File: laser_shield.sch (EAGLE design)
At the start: 18 parts, among them IC1 74AC08N, U1 ARDUINO_SHIELDLONGPADS

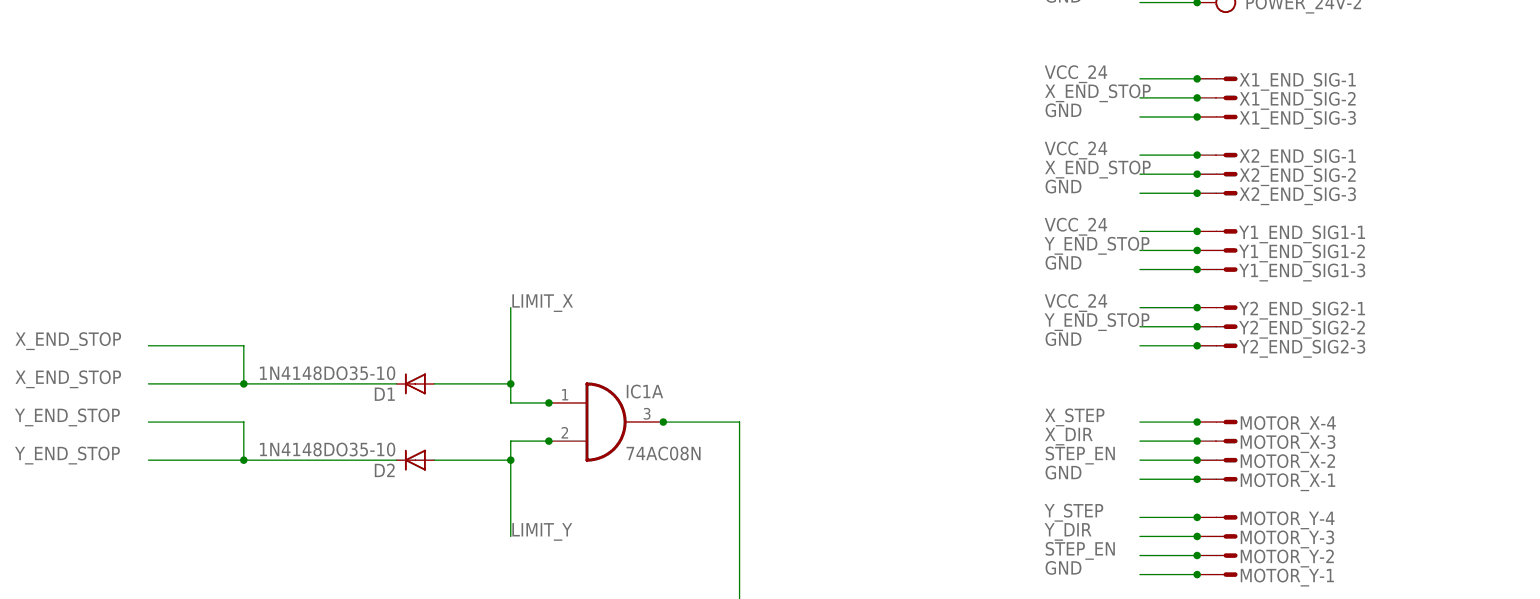
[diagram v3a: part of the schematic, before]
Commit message: Added Z_LIMIT
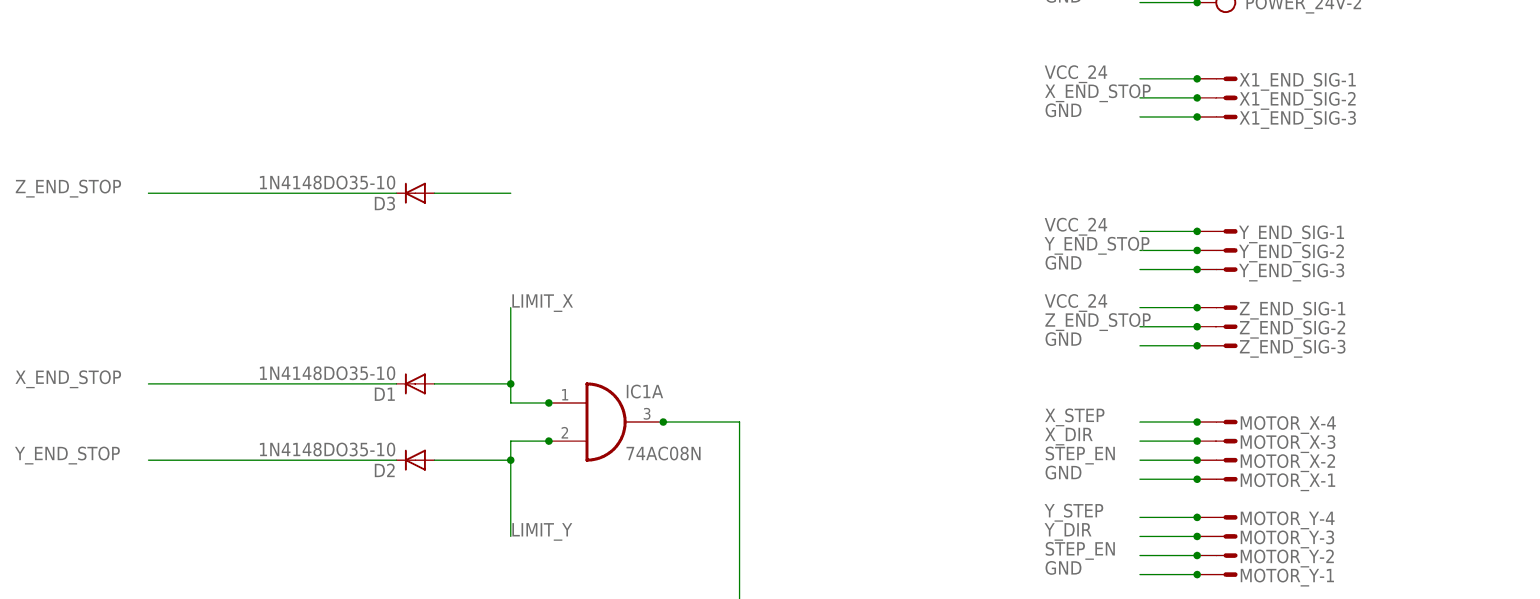
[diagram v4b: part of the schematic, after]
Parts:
- removed X2_END_SIG: (no value), con-amp-mt:L03P
- added D3: 1N4148DO35-10, diode:1N4148DO35-10
- renumbered Y1_END_SIG1 to Y_END_SIG, Y2_END_SIG2 to Z_END_SIG
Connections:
- new net Z_END_STOP: D3.C, Z_END_SIG-2.S
- net GND: no longer X2_END_SIG-3.S
- net LIMIT_Z: now also D3.A
- net VCC_24: no longer X2_END_SIG-1.S
- net X_END_STOP: no longer X2_END_SIG-2.S
- net Y_END_STOP: no longer Z_END_SIG-2.S
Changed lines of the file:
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@@
 <part name="LASER_OUT" library="con-amp-mt" deviceset="L03P" device=""/>
 <part name="RESET" library="con-amp-mt" deviceset="L02P" device=""/>
-<part name="X2_END_SIG" library="con-amp-mt" deviceset="L03P" device=""/>
 <part name="X1_END_SIG" library="con-amp-mt" deviceset="L03P" device=""/>
 <part name="IC1" library="74xx-eu" deviceset="74*08" device="N" technology="AC"/>
 <part name="PROBE" library="con-amp-mt" deviceset="L03P" device=""/>
-<part name="Y1_END_SIG1" library="con-amp-mt" deviceset="L03P" device=""/>
-<part name="Y2_END_SIG2" library="con-amp-mt" deviceset="L03P" device=""/>
+<part name="Y_END_SIG" library="con-amp-mt" deviceset="L03P" device=""/>
+<part name="Z_END_SIG" library="con-amp-mt" deviceset="L03P" device=""/>
 <part name="MOTOR_Z" library="con-amp-mt" deviceset="L04P" device=""/>
 <part name="FEED_H" library="con-amp-mt" deviceset="L02P" device=""/>
 <part name="CYCLE_S" library="con-amp-mt" deviceset="L02P" device=""/>
+<part name="D3" library="diode" deviceset="1N4148" device="DO35-10"/>
 </parts>
 <sheets>
@@
 <instance part="RESET" gate="-1" x="63.5" y="-10.16" rot="R180"/>
 <instance part="RESET" gate="-2" x="63.5" y="-7.62" rot="R180"/>
-<instance part="X2_END_SIG" gate="-1" x="63.5" y="101.6" rot="R180"/>
-<instance part="X2_END_SIG" gate="-2" x="63.5" y="99.06" rot="R180"/>
-<instance part="X2_END_SIG" gate="-3" x="63.5" y="96.52" rot="R180"/>
 <instance part="X1_END_SIG" gate="-1" x="63.5" y="111.76" rot="R180"/>
 <instance part="X1_END_SIG" gate="-2" x="63.5" y="109.22" rot="R180"/>
@@
 <instance part="PROBE" gate="-2" x="63.5" y="0" rot="R180"/>
 <instance part="PROBE" gate="-3" x="63.5" y="2.54" rot="R180"/>
-<instance part="Y1_END_SIG1" gate="-1" x="63.5" y="91.44" rot="R180"/>
-<instance part="Y1_END_SIG1" gate="-2" x="63.5" y="88.9" rot="R180"/>
-<instance part="Y1_END_SIG1" gate="-3" x="63.5" y="86.36" rot="R180"/>
-<instance part="Y2_END_SIG2" gate="-1" x="63.5" y="81.28" rot="R180"/>
-<instance part="Y2_END_SIG2" gate="-2" x="63.5" y="78.74" rot="R180"/>
-<instance part="Y2_END_SIG2" gate="-3" x="63.5" y="76.2" rot="R180"/>
+<instance part="Y_END_SIG" gate="-1" x="63.5" y="91.44" rot="R180"/>
+<instance part="Y_END_SIG" gate="-2" x="63.5" y="88.9" rot="R180"/>
+<instance part="Y_END_SIG" gate="-3" x="63.5" y="86.36" rot="R180"/>
+<instance part="Z_END_SIG" gate="-1" x="63.5" y="81.28" rot="R180"/>
+<instance part="Z_END_SIG" gate="-2" x="63.5" y="78.74" rot="R180"/>
+<instance part="Z_END_SIG" gate="-3" x="63.5" y="76.2" rot="R180"/>
 <instance part="MOTOR_Z" gate="-1" x="63.5" y="33.02" rot="R180"/>
 <instance part="MOTOR_Z" gate="-2" x="63.5" y="35.56" rot="R180"/>
@@
 <instance part="CYCLE_S" gate="-1" x="63.5" y="-25.4" rot="R180"/>
 <instance part="CYCLE_S" gate="-2" x="63.5" y="-22.86" rot="R180"/>
+<instance part="D3" gate="G$1" x="-45.72" y="96.52" rot="R180"/>
 </instances>
 <busses>
@@
 </segment>
 <segment>
-<wire x1="58.42" y1="96.52" x2="50.8" y2="96.52" width="0.1524" layer="91"/>
-<label x="38.1" y="96.52" size="1.778" layer="95"/>
-<pinref part="X2_END_SIG" gate="-3" pin="S"/>
-<junction x="58.42" y="96.52"/>
-</segment>
-<segment>
 <wire x1="58.42" y1="106.68" x2="50.8" y2="106.68" width="0.1524" layer="91"/>
 <label x="38.1" y="106.68" size="1.778" layer="95"/>
@@
 <wire x1="58.42" y1="76.2" x2="50.8" y2="76.2" width="0.1524" layer="91"/>
 <label x="38.1" y="76.2" size="1.778" layer="95"/>
-<pinref part="Y2_END_SIG2" gate="-3" pin="S"/>
+<pinref part="Z_END_SIG" gate="-3" pin="S"/>
 <junction x="58.42" y="76.2"/>
 </segment>
@@
 <wire x1="58.42" y1="86.36" x2="50.8" y2="86.36" width="0.1524" layer="91"/>
 <label x="38.1" y="86.36" size="1.778" layer="95"/>
-<pinref part="Y1_END_SIG1" gate="-3" pin="S"/>
+<pinref part="Y_END_SIG" gate="-3" pin="S"/>
 <junction x="58.42" y="86.36"/>
 </segment>
@@
 </segment>
 <segment>
-<wire x1="58.42" y1="101.6" x2="50.8" y2="101.6" width="0.1524" layer="91"/>
-<label x="38.1" y="101.6" size="1.778" layer="95"/>
-<pinref part="X2_END_SIG" gate="-1" pin="S"/>
-<junction x="58.42" y="101.6"/>
-</segment>
-<segment>
 <label x="38.1" y="91.44" size="1.778" layer="95"/>
 <wire x1="58.42" y1="91.44" x2="50.8" y2="91.44" width="0.1524" layer="91"/>
-<pinref part="Y1_END_SIG1" gate="-1" pin="S"/>
+<pinref part="Y_END_SIG" gate="-1" pin="S"/>
 <junction x="58.42" y="91.44"/>
 </segment>
@@
 <wire x1="58.42" y1="81.28" x2="50.8" y2="81.28" width="0.1524" layer="91"/>
 <label x="38.1" y="81.28" size="1.778" layer="95"/>
-<pinref part="Y2_END_SIG2" gate="-1" pin="S"/>
+<pinref part="Z_END_SIG" gate="-1" pin="S"/>
 <junction x="58.42" y="81.28"/>
 </segment>
@@
 <label x="167.64" y="22.86" size="1.778" layer="95"/>
 </segment>
+<segment>
+<pinref part="D3" gate="G$1" pin="A"/>
+<wire x1="-43.18" y1="96.52" x2="-33.02" y2="96.52" width="0.1524" layer="91"/>
+</segment>
 </net>
 <net name="SPINDLE_DIR" class="0">
@@
 <label x="38.1" y="88.9" size="1.778" layer="95"/>
 <wire x1="58.42" y1="88.9" x2="50.8" y2="88.9" width="0.1524" layer="91"/>
-<pinref part="Y1_END_SIG1" gate="-2" pin="S"/>
+<pinref part="Y_END_SIG" gate="-2" pin="S"/>
 <junction x="58.42" y="88.9"/>
 </segment>
 <segment>
-<wire x1="58.42" y1="78.74" x2="50.8" y2="78.74" width="0.1524" layer="91"/>
-<label x="38.1" y="78.74" size="1.778" layer="95"/>
-<pinref part="Y2_END_SIG2" gate="-2" pin="S"/>
-<junction x="58.42" y="78.74"/>
-</segment>
-<segment>
 <label x="-99.06" y="60.96" size="1.778" layer="95"/>
-<wire x1="-81.28" y1="66.04" x2="-68.58" y2="66.04" width="0.1524" layer="91"/>
-<label x="-99.06" y="66.04" size="1.778" layer="95"/>
-<wire x1="-81.28" y1="60.96" x2="-68.58" y2="60.96" width="0.1524" layer="91"/>
-<wire x1="-68.58" y1="66.04" x2="-68.58" y2="60.96" width="0.1524" layer="91"/>
-<wire x1="-68.58" y1="60.96" x2="-48.26" y2="60.96" width="0.1524" layer="91"/>
-<junction x="-68.58" y="60.96"/>
+<wire x1="-81.28" y1="60.96" x2="-48.26" y2="60.96" width="0.1524" layer="91"/>
 <pinref part="D2" gate="G$1" pin="C"/>
 </segment>
@@
 <net name="X_END_STOP" class="0">
 <segment>
-<wire x1="-68.58" y1="76.2" x2="-81.28" y2="76.2" width="0.1524" layer="91"/>
-<label x="-99.06" y="76.2" size="1.778" layer="95"/>
-<wire x1="-81.28" y1="71.12" x2="-68.58" y2="71.12" width="0.1524" layer="91"/>
 <label x="-99.06" y="71.12" size="1.778" layer="95"/>
-<wire x1="-68.58" y1="76.2" x2="-68.58" y2="71.12" width="0.1524" layer="91"/>
-<wire x1="-68.58" y1="71.12" x2="-48.26" y2="71.12" width="0.1524" layer="91"/>
-<junction x="-68.58" y="71.12"/>
+<wire x1="-81.28" y1="71.12" x2="-48.26" y2="71.12" width="0.1524" layer="91"/>
 <pinref part="D1" gate="G$1" pin="C"/>
 </segment>
@@
 <pinref part="X1_END_SIG" gate="-2" pin="S"/>
 <junction x="58.42" y="109.22"/>
-</segment>
-<segment>
-<wire x1="58.42" y1="99.06" x2="50.8" y2="99.06" width="0.1524" layer="91"/>
-<label x="38.1" y="99.06" size="1.778" layer="95"/>
-<pinref part="X2_END_SIG" gate="-2" pin="S"/>
-<junction x="58.42" y="99.06"/>
 </segment>
 </net>
@@
 </segment>
 </net>
+<net name="Z_END_STOP" class="0">
+<segment>
+<wire x1="58.42" y1="78.74" x2="50.8" y2="78.74" width="0.1524" layer="91"/>
+<label x="38.1" y="78.74" size="1.778" layer="95"/>
+<pinref part="Z_END_SIG" gate="-2" pin="S"/>
+<junction x="58.42" y="78.74"/>
+</segment>
+<segment>
+<label x="-99.06" y="96.52" size="1.778" layer="95"/>
+<wire x1="-81.28" y1="96.52" x2="-48.26" y2="96.52" width="0.1524" layer="91"/>
+<pinref part="D3" gate="G$1" pin="C"/>
+</segment>
+</net>
